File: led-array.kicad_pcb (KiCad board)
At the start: 4 copper layers, 180 x 105 mm, 1231 parts, among them J1 Conn_01x04_Pin, J2 USB_B_Micro, Q1 Q_NMOS_GDS, Q2 Q_NMOS_GDS, Q3 Q_NMOS_GDS, Q4 Q_NMOS_GDS, Q5 Q_NMOS_GDS, Q6 Q_NMOS_GDS, Q7 Q_NMOS_GDS, Q8 Q_NMOS_GDS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

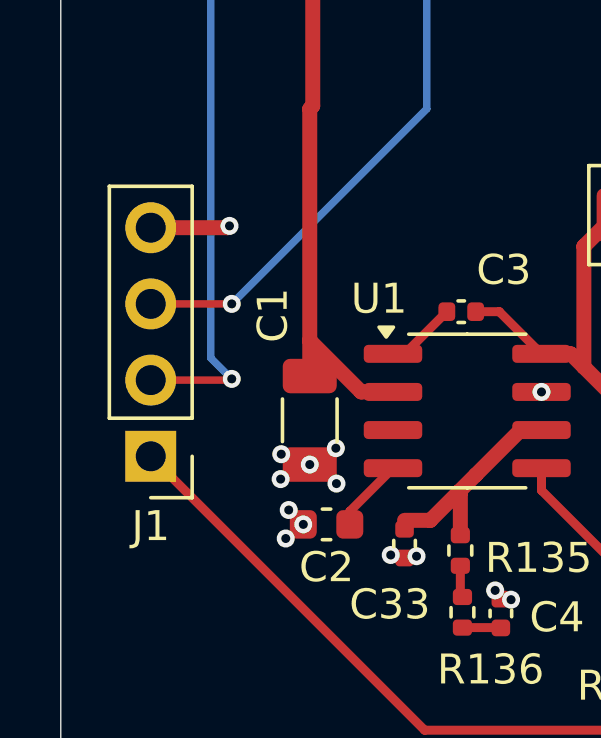
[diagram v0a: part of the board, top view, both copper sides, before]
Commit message: Modified pins to match JLCPCB layout
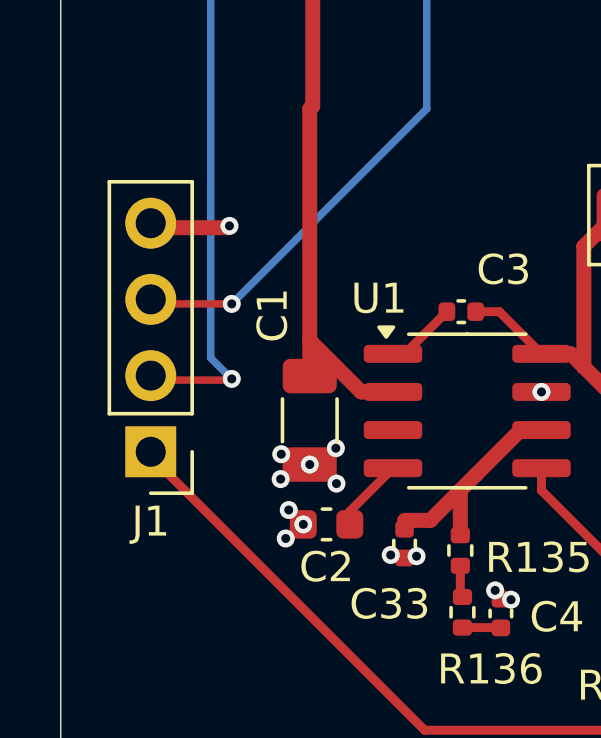
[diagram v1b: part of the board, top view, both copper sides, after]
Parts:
- moved J1 3.96 mm to (98.0, 174.6), turned to 90 degrees
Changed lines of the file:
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@@
 			(layers "*.Cu" "*.Mask")
 			(remove_unused_layers no)
-			(net 330 "unconnected-(J2-Shield-Pad6)")
+			(net 342 "unconnected-(J2-Shield-Pad6)_7")
 			(pinfunction "Shield")
 			(pintype "passive+no_connect")
@@
 			(size 1.2 1.9)
 			(layers "F.Cu" "F.Mask")
-			(net 331 "unconnected-(J2-Shield-Pad6)_1")
+			(net 341 "unconnected-(J2-Shield-Pad6)_6")
 			(pinfunction "Shield")
 			(pintype "passive+no_connect")
@@
 			(layers "*.Cu" "*.Mask")
 			(remove_unused_layers no)
-			(net 332 "unconnected-(J2-Shield-Pad6)_2")
+			(net 340 "unconnected-(J2-Shield-Pad6)_5")
 			(pinfunction "Shield")
 			(pintype "passive+no_connect")
@@
 			(size 1.5 1.9)
 			(layers "F.Cu" "F.Mask" "F.Paste")
-			(net 333 "unconnected-(J2-Shield-Pad6)_3")
+			(net 339 "unconnected-(J2-Shield-Pad6)_4")
 			(pinfunction "Shield")
 			(pintype "passive+no_connect")
@@
 			(size 1.5 1.9)
 			(layers "F.Cu" "F.Mask" "F.Paste")
-			(net 339 "unconnected-(J2-Shield-Pad6)_4")
+			(net 333 "unconnected-(J2-Shield-Pad6)_3")
 			(pinfunction "Shield")
 			(pintype "passive+no_connect")
@@
 			(layers "*.Cu" "*.Mask")
 			(remove_unused_layers no)
-			(net 340 "unconnected-(J2-Shield-Pad6)_5")
+			(net 332 "unconnected-(J2-Shield-Pad6)_2")
 			(pinfunction "Shield")
 			(pintype "passive+no_connect")
@@
 			(size 1.2 1.9)
 			(layers "F.Cu" "F.Mask")
-			(net 341 "unconnected-(J2-Shield-Pad6)_6")
+			(net 331 "unconnected-(J2-Shield-Pad6)_1")
 			(pinfunction "Shield")
 			(pintype "passive+no_connect")
@@
 			(layers "*.Cu" "*.Mask")
 			(remove_unused_layers no)
-			(net 342 "unconnected-(J2-Shield-Pad6)_7")
+			(net 330 "unconnected-(J2-Shield-Pad6)")
 			(pinfunction "Shield")
 			(pintype "passive+no_connect")
@@
 	(footprint "Connector_PinHeader_2.54mm:PinHeader_1x04_P2.54mm_Vertical"
 		(layer "F.Cu")
-		(at 98 178.58 180)
+		(at 98 174.62 90)
 		(descr "Through hole straight pin header, 1x04, 2.54mm pitch, single row")
 		(tags "Through hole pin header THT 1x04 2.54mm single row")
 		(property "Reference" "J1"
-			(at 0 -2.33 0)
+			(at -6.14 0 0)
 			(layer "F.SilkS")
 			(effects
@@
 		)
 		(property "Value" "Conn_01x04_Pin"
-			(at 0 9.95 0)
+			(at 6.14 0 0)
 			(layer "F.Fab")
 			(effects
@@
 		)
 		(property "Datasheet" "~"
-			(at 0 0 180)
+			(at 0 0 90)
 			(unlocked yes)
 			(layer "F.Fab")
@@
 		)
 		(property "Description" "Generic connector, single row, 01x04, script generated"
-			(at 0 0 180)
+			(at 0 0 90)
 			(unlocked yes)
 			(layer "F.Fab")
@@
 		)
 		(property "LCSC" "C5116483"
-			(at 0 0 180)
+			(at 0 0 90)
 			(unlocked yes)
 			(layer "F.Fab")
@@
 		(attr through_hole)
 		(fp_line
-			(start 1.38 1.27)
-			(end 1.38 9)
+			(start -2.54 -1.38)
+			(end 5.19 -1.38)
 			(stroke
 				(width 0.12)
@@
 		)
 		(fp_line
-			(start -1.38 9)
-			(end 1.38 9)
+			(start 5.19 1.38)
+			(end 5.19 -1.38)
 			(stroke
 				(width 0.12)
@@
 		)
 		(fp_line
-			(start -1.38 1.27)
-			(end 1.38 1.27)
+			(start -2.54 1.38)
+			(end -2.54 -1.38)
 			(stroke
 				(width 0.12)
@@
 		)
 		(fp_line
-			(start -1.38 1.27)
-			(end -1.38 9)
+			(start -2.54 1.38)
+			(end 5.19 1.38)
 			(stroke
 				(width 0.12)
@@
 		)
 		(fp_line
-			(start -1.38 0)
-			(end -1.38 -1.38)
+			(start -3.81 1.38)
+			(end -5.19 1.38)
 			(stroke
 				(width 0.12)
@@
 		)
 		(fp_line
-			(start -1.38 -1.38)
-			(end 0 -1.38)
+			(start -5.19 1.38)
+			(end -5.19 0)
 			(stroke
 				(width 0.12)
@@
 		)
 		(fp_line
-			(start 1.77 9.39)
-			(end 1.77 -1.77)
+			(start 5.58 -1.77)
+			(end -5.58 -1.77)
 			(stroke
 				(width 0.05)
@@
 		)
 		(fp_line
-			(start 1.77 -1.77)
-			(end -1.77 -1.77)
+			(start -5.58 -1.77)
+			(end -5.58 1.77)
 			(stroke
 				(width 0.05)
@@
 		)
 		(fp_line
-			(start -1.77 9.39)
-			(end 1.77 9.39)
+			(start 5.58 1.77)
+			(end 5.58 -1.77)
 			(stroke
 				(width 0.05)
@@
 		)
 		(fp_line
-			(start -1.77 -1.77)
-			(end -1.77 9.39)
+			(start -5.58 1.77)
+			(end 5.58 1.77)
 			(stroke
 				(width 0.05)
@@
 		)
 		(fp_line
-			(start 1.27 8.89)
-			(end -1.27 8.89)
+			(start 5.08 -1.27)
+			(end 5.08 1.27)
 			(stroke
 				(width 0.1)
@@
 		)
 		(fp_line
-			(start 1.27 -1.27)
-			(end 1.27 8.89)
+			(start -5.08 -1.27)
+			(end 5.08 -1.27)
 			(stroke
 				(width 0.1)
@@
 		)
 		(fp_line
-			(start -0.635 -1.27)
-			(end 1.27 -1.27)
+			(start -5.08 0.635)
+			(end -5.08 -1.27)
 			(stroke
 				(width 0.1)
@@
 		)
 		(fp_line
-			(start -1.27 8.89)
-			(end -1.27 -0.635)
+			(start 5.08 1.27)
+			(end -4.445 1.27)
 			(stroke
 				(width 0.1)
@@
 		)
 		(fp_line
-			(start -1.27 -0.635)
-			(end -0.635 -1.27)
+			(start -4.445 1.27)
+			(end -5.08 0.635)
 			(stroke
 				(width 0.1)
@@
 		)
 		(fp_text user "${REFERENCE}"
-			(at 0 3.81 90)
+			(at 0 0 90)
 			(layer "F.Fab")
 			(effects
@@
 		)
 		(pad "1" thru_hole rect
-			(at 0 0 180)
+			(at -3.81 0 180)
 			(size 1.7 1.7)
 			(drill 1)
@@
 		)
 		(pad "2" thru_hole circle
-			(at 0 2.54 180)
+			(at -1.27 0 180)
 			(size 1.7 1.7)
 			(drill 1)
@@
 		)
 		(pad "3" thru_hole circle
-			(at 0 5.08 180)
+			(at 1.27 0 180)
 			(size 1.7 1.7)
 			(drill 1)
@@
 		)
 		(pad "4" thru_hole circle
-			(at 0 7.62 180)
+			(at 3.81 0 180)
 			(size 1.7 1.7)
 			(drill 1)
